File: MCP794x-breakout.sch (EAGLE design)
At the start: 11 parts, among them U4 MCP794x, X3 53261-02, Y2 ABS07

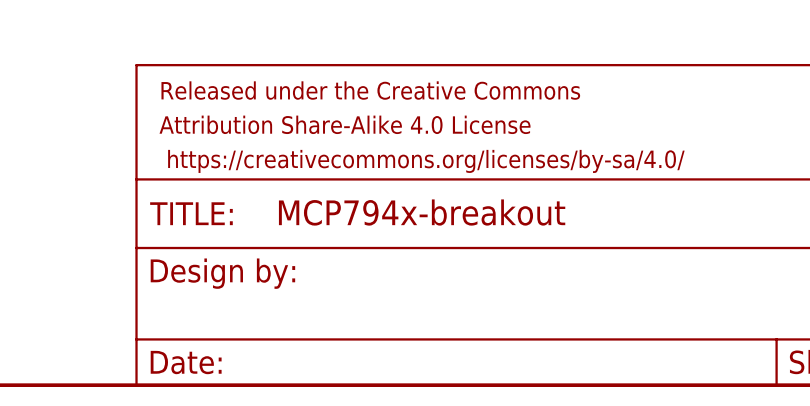
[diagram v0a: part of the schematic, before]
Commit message: labels fixed
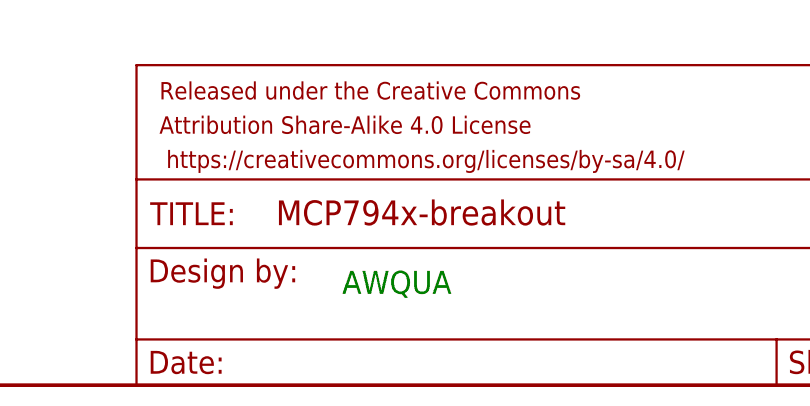
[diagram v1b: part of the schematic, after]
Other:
- note added: "AWQUA"
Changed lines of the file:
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@@
 <sheet>
 <plain>
+<text x="170.18" y="10.16" size="2.54" layer="91">AWQUA</text>
 </plain>
 <instances>
